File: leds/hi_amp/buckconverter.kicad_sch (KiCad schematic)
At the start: 12 parts, among them U5 TPS54202DDC, U6 CYA1040-15UH

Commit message: WIP hi_amp leds
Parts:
- removed C21, C22: 22uF, Capacitor_SMD:C_Elec_5x5.8, symbol Device:C_Polarized
- removed TP4: LabeledTestPoint, easyeda2kicad:LabeledTestPoint, symbol easyeda2kicad:LabeledTestPoint
- removed U6: CYA1040-15UH, easyeda2kicad:IND-SMD_L11.6-W10.1, symbol easyeda2kicad:CYA1040-15UH
- added C10, C11, C6: 22uF, Capacitor_SMD:C_1206_3216Metric, symbol Device:C
- added L1: XGL4040-153MEC, easyeda2kicad:IND-SMD_L4.0-W4.0_XAL4040-103, symbol easyeda2kicad:XGL4040-153MEC
- renumbered C23 to C12, C18 to C7, C19 to C8, C20 to C9, R18 to R10, R19 to R11, R20 to R12, U5 to U3
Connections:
- net GND: now also C10.2, C11.2, C6.2
- net SW: now also L1.1
- net VIN: now also C6.1
- net VOUT: now also C10.1, C11.1, L1.2
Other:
- moved on the sheet: C12, C7, C8, C9, R10, R11, R12, U3

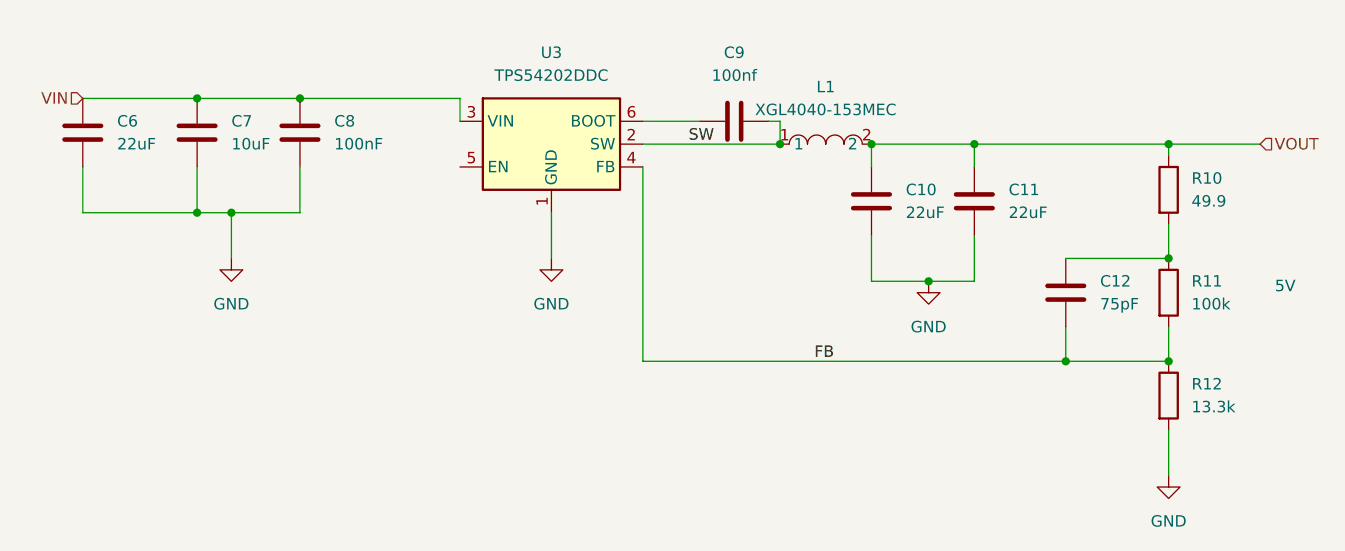
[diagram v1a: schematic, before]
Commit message: WIP: add vias to buck (after fabrication).
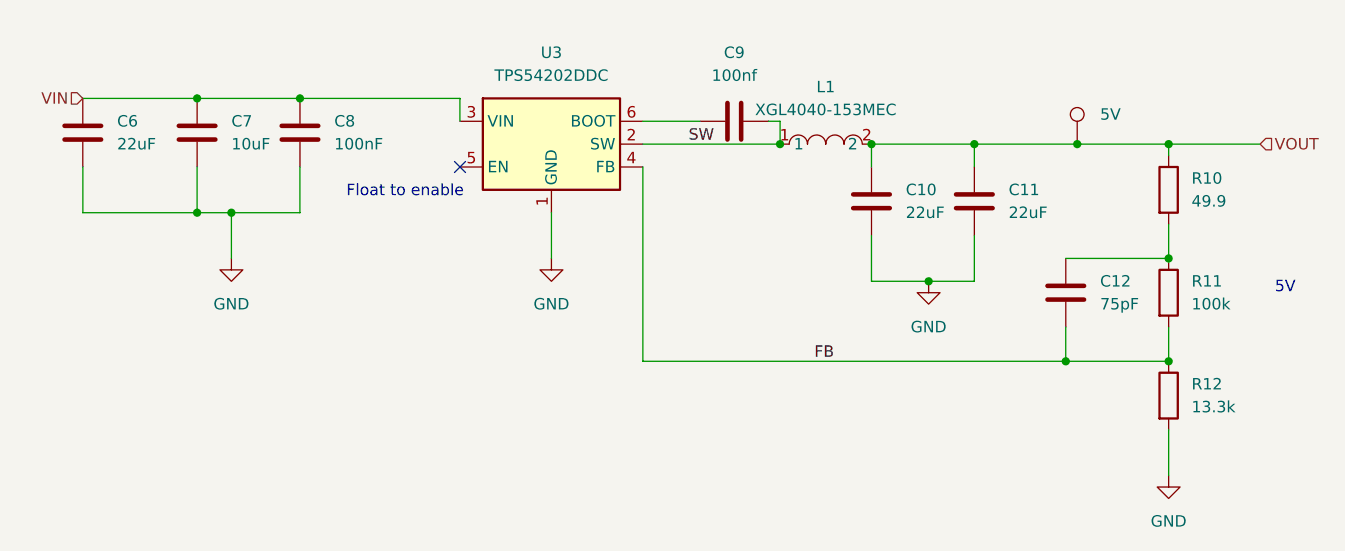
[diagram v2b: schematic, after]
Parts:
- added TP301: LabeledTestPoint, easyeda2kicad:LabeledTestPoint, symbol easyeda2kicad:LabeledTestPoint
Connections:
- net VOUT: now also TP301.1
- no-connect marks 0 -> 1
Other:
- note added: "Float to enable"
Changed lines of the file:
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@@
+		)
+	)
+	(text "Float to enable"
+		(exclude_from_sim no)
+		(at 58.674 38.354 0)
+		(effects
+			(font
+				(size 1.27 1.27)
+			)
 		)
 	)
@@
 	)
 	(junction
+		(at 133.35 33.02)
+		(diameter 0)
+		(color 0 0 0 0)
+	)
+	(junction
 		(at 46.99 27.94)
 		(diameter 0)
@@
 		(color 0 0 0 0)
 	)
+	(no_connect
+		(at 64.77 35.56)
+	)
 	(wire
 		(pts
@@
 	(wire
 		(pts
+			(xy 133.35 33.02) (xy 143.51 33.02)
+		)
+		(stroke
+			(width 0)
+			(type default)
+		)
+	)
+	(wire
+		(pts
 			(xy 35.56 40.64) (xy 39.37 40.64)
 		)
@@
 	(wire
 		(pts
-			(xy 121.92 33.02) (xy 143.51 33.02)
+			(xy 121.92 33.02) (xy 133.35 33.02)
 		)
 		(stroke
@@
 					(unit 1)
 				)
+			)
+		)
+	)
+	(symbol
+		(lib_id "easyeda2kicad:LabeledTestPoint")
+		(at 133.35 33.02 0)
+		(unit 1)
+		(exclude_from_sim no)
+		(in_bom no)
+		(on_board yes)
+		(dnp no)
+		(fields_autoplaced yes)
+		(property "Reference" "TP301"
+			(at 133.35 26.162 0)
+			(effects
+				(font
+					(size 1.27 1.27)
+				)
+				(hide yes)
+			)
+		)
+		(property "Value" "LabeledTestPoint"
+			(at 133.35 27.94 0)
+			(effects
+				(font
+					(size 1.27 1.27)
+				)
+				(hide yes)
+			)
+		)
+		(property "Footprint" "easyeda2kicad:LabeledTestPoint"
+			(at 138.43 33.02 0)
+			(effects
+				(font
+					(size 1.27 1.27)
+				)
+				(hide yes)
+			)
+		)
+		(property "Datasheet" "~"
+			(at 138.43 33.02 0)
+			(effects
+				(font
+					(size 1.27 1.27)
+				)
+				(hide yes)
+			)
+		)
+		(property "Description" "test point"
+			(at 133.35 33.02 0)
+			(effects
+				(font
+					(size 1.27 1.27)
+				)
+				(hide yes)
+			)
+		)
+		(property "Label" "5V"
+			(at 135.89 29.7179 0)
+			(effects
+				(font
+					(size 1.27 1.27)
+				)
+				(justify left)
+			)
+		)
+		(pin "1"
+		)
+		(instances
+			(project ""
+				(path "/48ddfdd8-68fa-4e63-aa18-bc113cdf8cfa/aa9739d0-05d8-4c74-a4fd-846c263eed0b"
+					(reference "TP301")
+					(unit 1)
+				)

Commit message: add stronger gate driver to LEDs
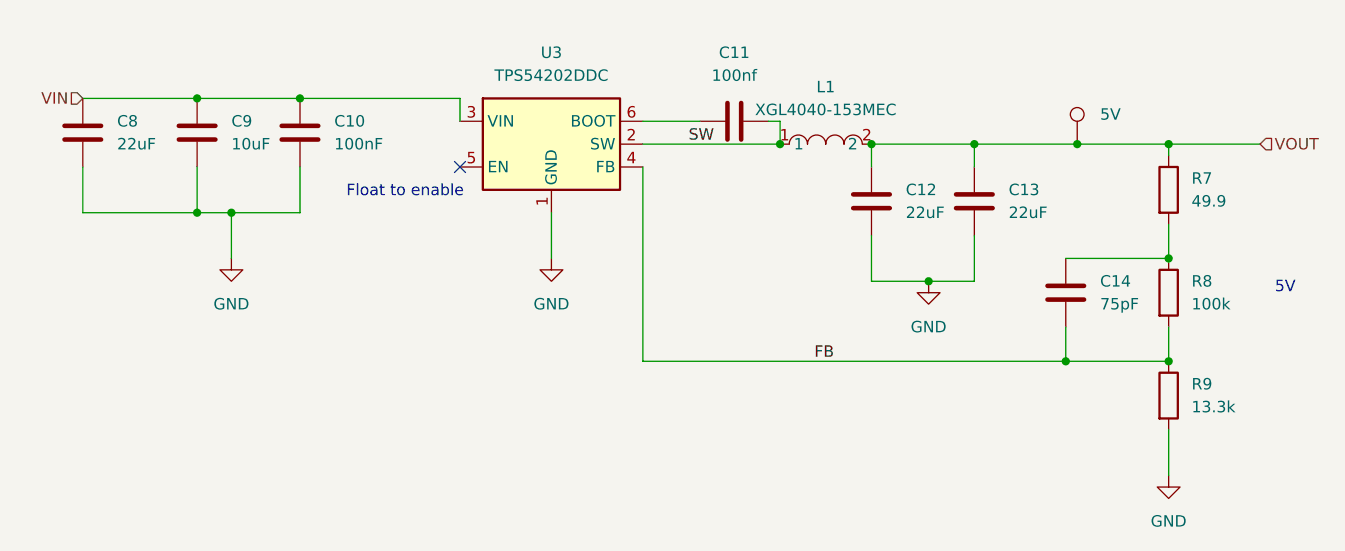
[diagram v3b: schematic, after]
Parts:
- renumbered C8 to C10, C9 to C11, C10 to C12, C11 to C13, C12 to C14, C6 to C8, C7 to C9, R10 to R7, R11 to R8, R12 to R9, TP301 to TP14
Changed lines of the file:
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@@
 		(dnp no)
 		(fields_autoplaced yes)
-		(property "Reference" "#PWR015"
+		(property "Reference" "#PWR016"
 			(at 143.51 76.2 0)
 			(effects
@@
 			(project "hi_amp"
 				(path "/48ddfdd8-68fa-4e63-aa18-bc113cdf8cfa/aa9739d0-05d8-4c74-a4fd-846c263eed0b"
-					(reference "#PWR015")
+					(reference "#PWR016")
 					(unit 1)
 				)
@@
 		(dnp no)
 		(fields_autoplaced yes)
-		(property "Reference" "#PWR012"
+		(property "Reference" "#PWR013"
 			(at 39.37 52.07 0)
 			(effects
@@
 			(project "hi_amp"
 				(path "/48ddfdd8-68fa-4e63-aa18-bc113cdf8cfa/aa9739d0-05d8-4c74-a4fd-846c263eed0b"
-					(reference "#PWR012")
+					(reference "#PWR013")
 					(unit 1)
 				)
@@
 		(dnp no)
 		(fields_autoplaced yes)
-		(property "Reference" "R11"
+		(property "Reference" "R8"
 			(at 146.05 48.2599 0)
 			(effects
@@
 			(project "hi_amp"
 				(path "/48ddfdd8-68fa-4e63-aa18-bc113cdf8cfa/aa9739d0-05d8-4c74-a4fd-846c263eed0b"
-					(reference "R11")
+					(reference "R8")
 					(unit 1)
 				)
@@
 		(dnp no)
 		(fields_autoplaced yes)
-		(property "Reference" "C12"
+		(property "Reference" "C14"
 			(at 135.89 48.2599 0)
 			(effects
@@
 			(project "hi_amp"
 				(path "/48ddfdd8-68fa-4e63-aa18-bc113cdf8cfa/aa9739d0-05d8-4c74-a4fd-846c263eed0b"
-					(reference "C12")
+					(reference "C14")
 					(unit 1)
 				)
@@
 		(dnp no)
 		(fields_autoplaced yes)
-		(property "Reference" "C8"
+		(property "Reference" "C10"
 			(at 50.8 30.4799 0)
 			(effects
@@
 			(project "hi_amp"
 				(path "/48ddfdd8-68fa-4e63-aa18-bc113cdf8cfa/aa9739d0-05d8-4c74-a4fd-846c263eed0b"
-					(reference "C8")
+					(reference "C10")
 					(unit 1)
 				)
@@
 		(dnp no)
 		(fields_autoplaced yes)
-		(property "Reference" "R10"
+		(property "Reference" "R7"
 			(at 146.05 36.8299 0)
 			(effects
@@
 			(project "hi_amp"
 				(path "/48ddfdd8-68fa-4e63-aa18-bc113cdf8cfa/aa9739d0-05d8-4c74-a4fd-846c263eed0b"
-					(reference "R10")
+					(reference "R7")
 					(unit 1)
 				)
@@
 		(dnp no)
 		(fields_autoplaced yes)
-		(property "Reference" "C10"
+		(property "Reference" "C12"
 			(at 114.3 38.0999 0)
 			(effects
@@
 			(project "hi_amp"
 				(path "/48ddfdd8-68fa-4e63-aa18-bc113cdf8cfa/aa9739d0-05d8-4c74-a4fd-846c263eed0b"
-					(reference "C10")
+					(reference "C12")
 					(unit 1)
 				)
@@
 		(dnp no)
 		(fields_autoplaced yes)
-		(property "Reference" "C11"
+		(property "Reference" "C13"
 			(at 125.73 38.0999 0)
 			(effects
@@
 			(project "hi_amp"
 				(path "/48ddfdd8-68fa-4e63-aa18-bc113cdf8cfa/aa9739d0-05d8-4c74-a4fd-846c263eed0b"
-					(reference "C11")
+					(reference "C13")
 					(unit 1)
 				)
@@
 		(dnp no)
 		(fields_autoplaced yes)
-		(property "Reference" "C7"
+		(property "Reference" "C9"
 			(at 39.37 30.4799 0)
 			(effects
@@
 			(project "hi_amp"
 				(path "/48ddfdd8-68fa-4e63-aa18-bc113cdf8cfa/aa9739d0-05d8-4c74-a4fd-846c263eed0b"
-					(reference "C7")
+					(reference "C9")
 					(unit 1)
 				)
@@
 		(dnp no)
 		(fields_autoplaced yes)
-		(property "Reference" "#PWR014"
+		(property "Reference" "#PWR015"
 			(at 116.84 54.61 0)
 			(effects
@@
 			(project "hi_amp"
 				(path "/48ddfdd8-68fa-4e63-aa18-bc113cdf8cfa/aa9739d0-05d8-4c74-a4fd-846c263eed0b"
-					(reference "#PWR014")
+					(reference "#PWR015")
 					(unit 1)
 				)
@@
 		(dnp no)
 		(fields_autoplaced yes)
-		(property "Reference" "C6"
+		(property "Reference" "C8"
 			(at 26.67 30.4799 0)
 			(effects
@@
 			(project "hi_amp"
 				(path "/48ddfdd8-68fa-4e63-aa18-bc113cdf8cfa/aa9739d0-05d8-4c74-a4fd-846c263eed0b"
-					(reference "C6")
+					(reference "C8")
 					(unit 1)
 				)
@@
 		(dnp no)
 		(fields_autoplaced yes)
-		(property "Reference" "TP301"
+		(property "Reference" "TP14"
 			(at 133.35 26.162 0)
 			(effects
@@
 			(project ""
 				(path "/48ddfdd8-68fa-4e63-aa18-bc113cdf8cfa/aa9739d0-05d8-4c74-a4fd-846c263eed0b"
-					(reference "TP301")
+					(reference "TP14")
 					(unit 1)
 				)
@@
 		(dnp no)
 		(fields_autoplaced yes)
-		(property "Reference" "C9"
+		(property "Reference" "C11"
 			(at 95.25 22.86 90)
 			(effects
@@
 			(project "hi_amp"
 				(path "/48ddfdd8-68fa-4e63-aa18-bc113cdf8cfa/aa9739d0-05d8-4c74-a4fd-846c263eed0b"
-					(reference "C9")
+					(reference "C11")
 					(unit 1)
 				)
@@
 		(dnp no)
 		(fields_autoplaced yes)
-		(property "Reference" "R12"
+		(property "Reference" "R9"
 			(at 146.05 59.6899 0)
 			(effects
@@
 			(project "hi_amp"
 				(path "/48ddfdd8-68fa-4e63-aa18-bc113cdf8cfa/aa9739d0-05d8-4c74-a4fd-846c263eed0b"
-					(reference "R12")
+					(reference "R9")
 					(unit 1)
 				)
@@
 		(dnp no)
 		(fields_autoplaced yes)
-		(property "Reference" "#PWR013"
+		(property "Reference" "#PWR014"
 			(at 74.93 52.07 0)
 			(effects
@@
 			(project "hi_amp"
 				(path "/48ddfdd8-68fa-4e63-aa18-bc113cdf8cfa/aa9739d0-05d8-4c74-a4fd-846c263eed0b"
-					(reference "#PWR013")
-					(unit 1)
-				)
+					(reference "#PWR014")
+					(unit 1)
+				)
